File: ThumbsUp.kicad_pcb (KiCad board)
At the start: 2 copper layers, 215.3 x 230 mm, 51 parts, among them J1 52559-1233, J1L1 PJ-3200B, J1R1 PJ-3200B, J2 52559-1233, U1 ProMicro

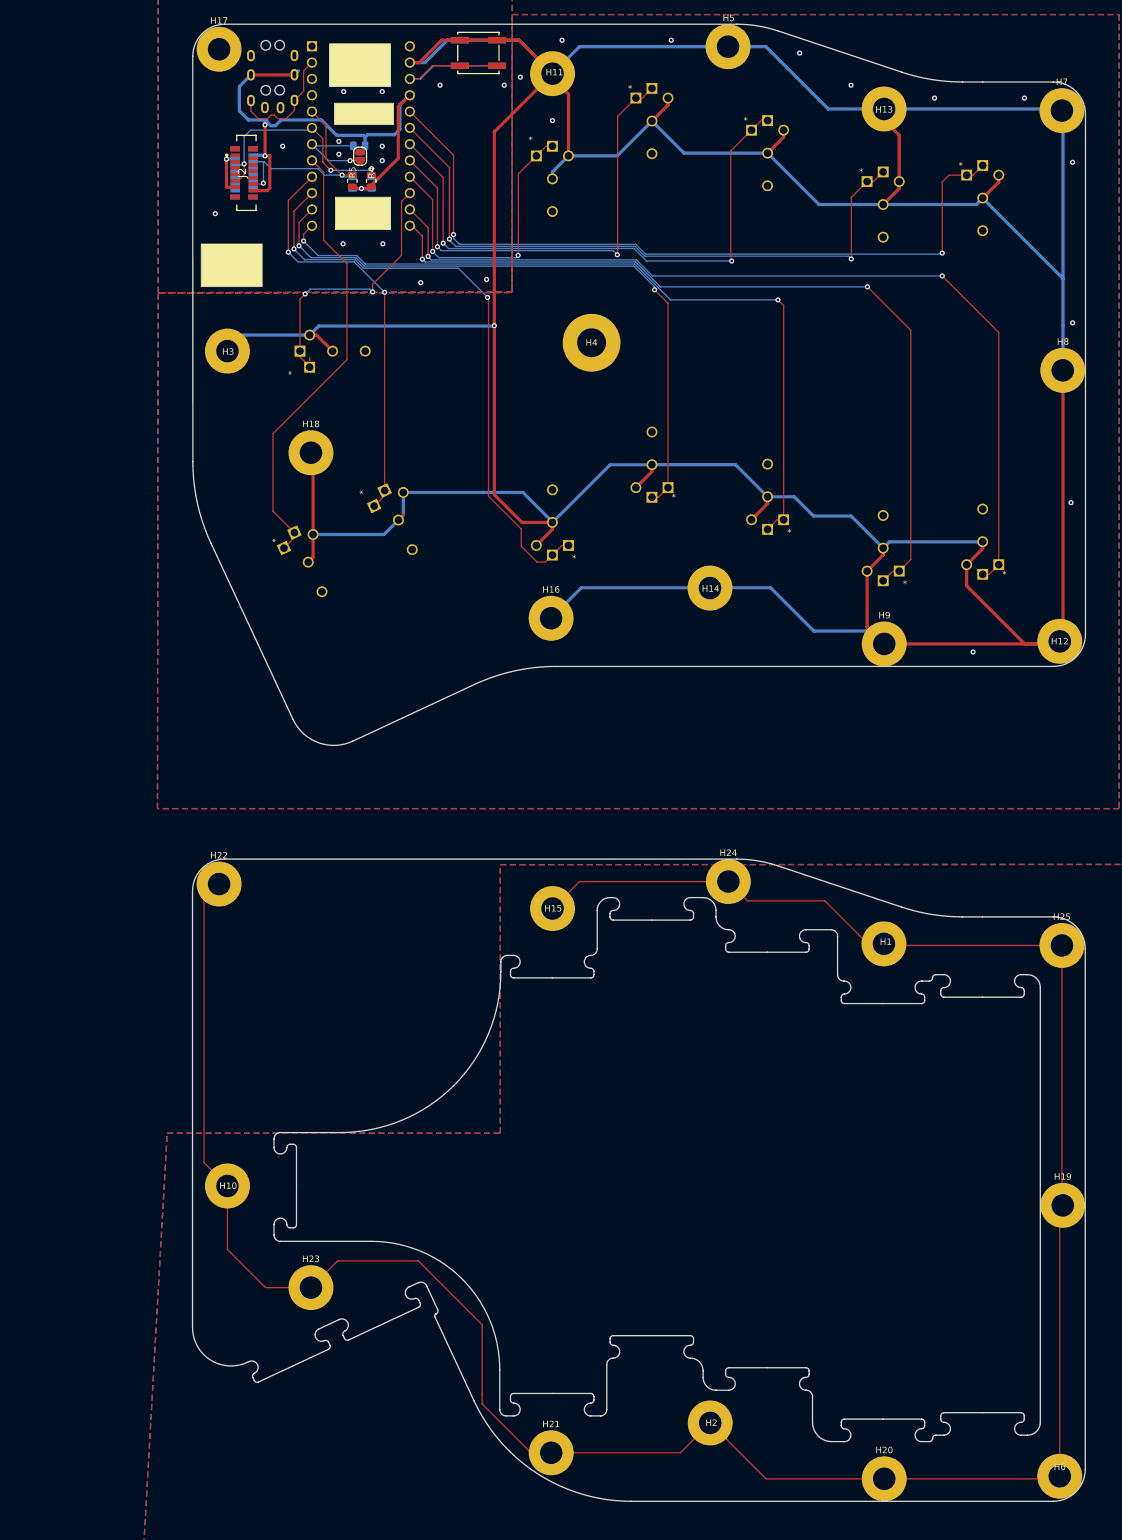
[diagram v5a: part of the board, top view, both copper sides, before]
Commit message: v12: Moving the thumb keys around.
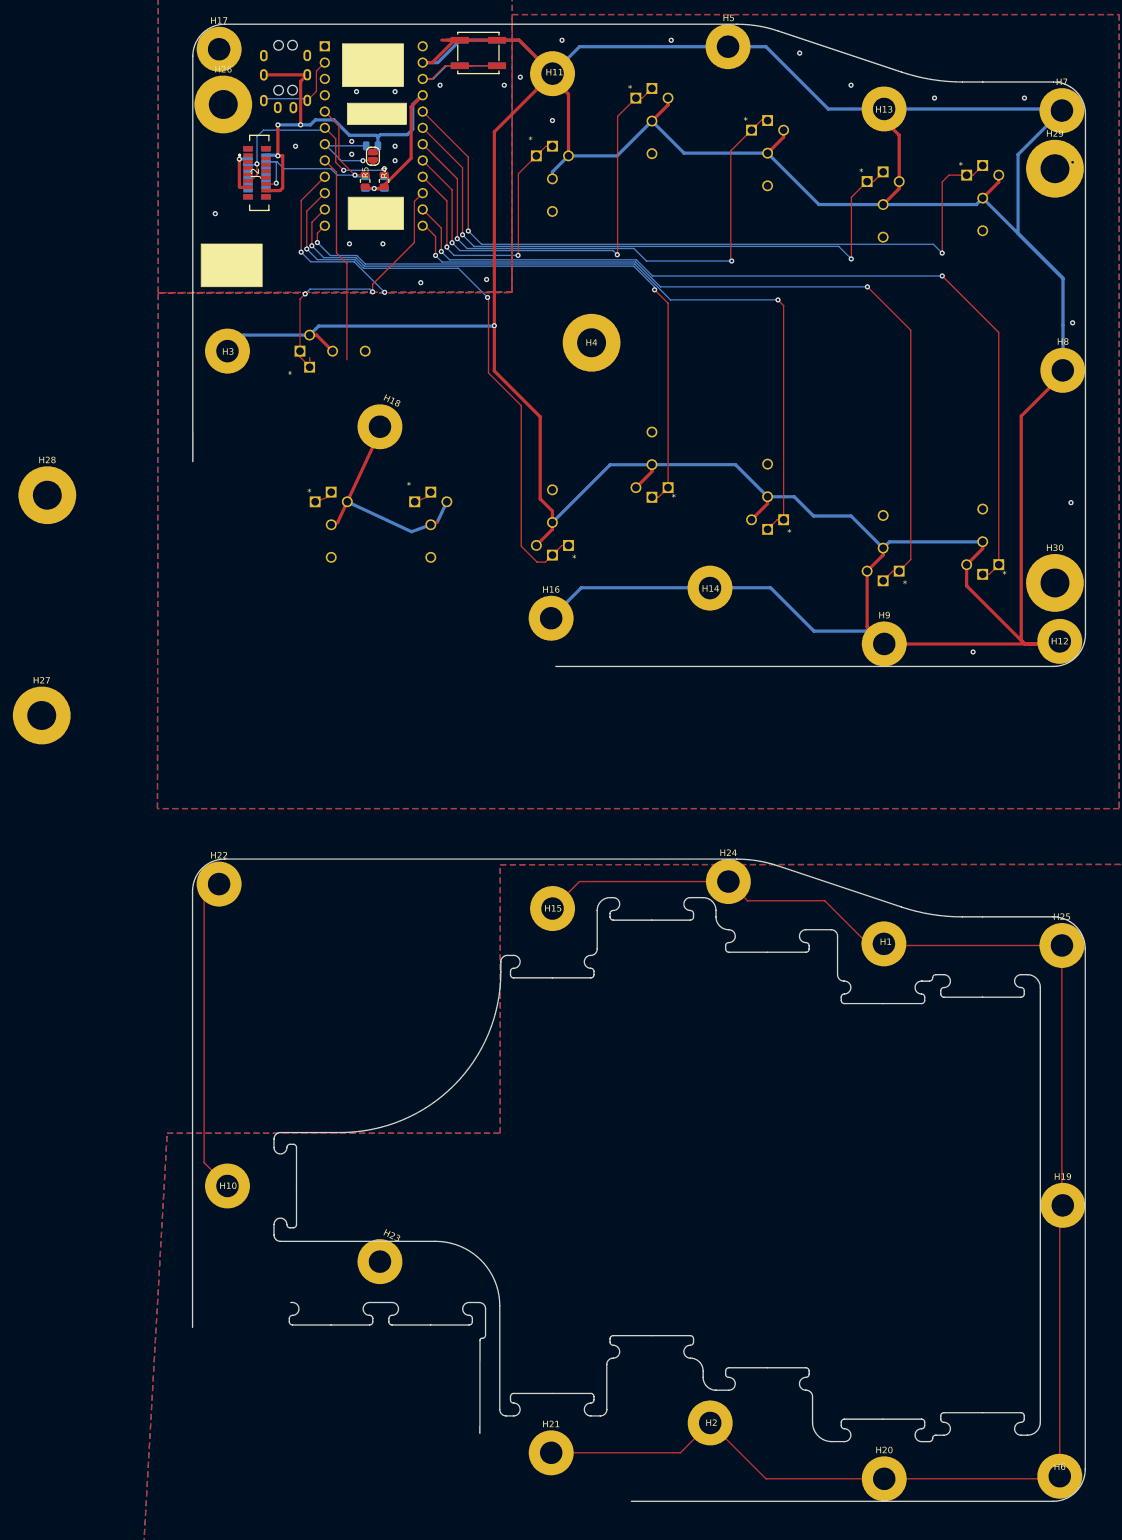
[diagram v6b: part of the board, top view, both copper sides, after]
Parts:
- added H26: MountingHole_Pad, MountingHole:MountingHole_4.5mm_Pad, F.Cu at (36.2, 38.0)
- added H27: MountingHole_Pad, MountingHole:MountingHole_4.5mm_Pad, F.Cu at (7.98, 133.1)
- added H28: MountingHole_Pad, MountingHole:MountingHole_4.5mm_Pad, F.Cu at (8.85, 98.8)
- added H29: MountingHole_Pad, MountingHole:MountingHole_4.5mm_Pad, F.Cu at (165.8, 48.0)
- added H30: MountingHole_Pad, MountingHole:MountingHole_4.5mm_Pad, F.Cu at (165.8, 112.5)
- moved H23 11.5 mm to (60.6, 218.2), turned to -25 degrees
- moved H18 11.5 mm to (60.6, 88.2), turned to -25 degrees
- moved MX30 8.52 mm to (53.1, 98.4), turned to 0 degrees
- moved MX26 7.19 mm to (68.6, 98.4), turned to 0 degrees
- moved J1 2.00 mm to (41.5, 48.6)
- moved J1L1 2.00 mm to (47.0, 27.2)
- moved J1R1 2.00 mm to (44.9, 27.2)
- moved J2 2.00 mm to (41.5, 48.6)
- moved JP1 2.00 mm to (59.6, 46.0)
- moved R1 2.00 mm to (58.4, 50.2)
- moved R17 2.00 mm to (59.4, 44.4)
- moved R2 2.00 mm to (61.3, 50.2)
- moved R4 2.00 mm to (61.3, 49.9)
- moved R5 2.00 mm to (58.3, 49.9)
- moved U1 2.00 mm to (59.7, 42.9)
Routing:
- net GNDA: track 389.6 -> 305.6 mm
- net SwE: track 69.4 -> 35.5 mm
- net SwU: track 64.8 -> 31.9 mm
- net GND: track 785.1 -> 765.4 mm
- net L-RING1: track 90.1 -> 84.9 mm, vias 3 -> 4
- net L-TIP: track 18.5 -> 14.0 mm
- net SwD: track 118.2 -> 115.2 mm
- net SwF: track 46.8 -> 43.9 mm
- net SwZ: track 141.8 -> 139.1 mm
- net SwL: track 88.6 -> 85.9 mm
- net SwP: track 72.5 -> 69.9 mm
- net SwT: track 100.0 -> 97.5 mm
- net SwS: track 128.2 -> 125.8 mm
- net SwG: track 118.3 -> 116.2 mm
- net SwR: track 93.2 -> 91.2 mm
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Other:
- outline, holes or cut-outs redrawn
- board text added: "u/ak66666 ThumbsUp! v.12 rev.5 June 2026"
- board text removed: "Raiser_Female"
- board text removed: "u/ak66666 ThumbsUp! v.12 rev.3 March 2026"

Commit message: v12: Added stand-offs instead of pin headers/sockets.
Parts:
- removed H29, H30: MountingHole_Pad, MountingHole:MountingHole_4.5mm_Pad
- added H31: MountingHole_Pad, MountingHole:MountingHole_3.5mm_Pad, F.Cu at (103.0, 26.4)
- added H32: MountingHole_Pad, MountingHole:MountingHole_3.5mm_Pad, F.Cu at (103.0, 108.2)
- added H33: MountingHole_Pad, MountingHole:MountingHole_3.5mm_Pad, F.Cu at (103.0, 156.4)
- added H34: MountingHole_Pad, MountingHole:MountingHole_3.5mm_Pad, F.Cu at (103.0, 238.2)
- moved H8 103.0 mm to (64.5, 88.9), turned to 15 degrees
- moved H19 102.9 mm to (64.5, 219.0), turned to 15 degrees
- moved H27 47.0 mm to (54.9, 130.6)
- moved H28 43.9 mm to (40.1, 68.0)
- moved H25 12.4 mm to (154.5, 169.4)
- moved H7 12.4 mm to (154.5, 39.5)
- moved H18 12.1 mm to (49.5, 93.0), turned to -10 degrees
- moved H23 12.1 mm to (49.6, 223.0), turned to -10 degrees
- moved H6 12.0 mm to (154.5, 251.2)
- moved H12 12.0 mm to (154.5, 121.2)
- moved H14 8.93 mm to (121.0, 113.2)
- moved H2 8.89 mm to (121.0, 243.1)
- moved H24 6.55 mm to (121.0, 161.4)
- moved H5 6.50 mm to (121.0, 31.4)
- moved H17 4.00 mm to (39.6, 29.4)
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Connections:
- H2 pad 1: GNDA -> GNDC
- H20 pad 1: GNDA -> GNDC
- H21 pad 1: GNDA -> GNDC
- H27 pad 1: GND-B -> GND
- H28 pad 1: GND-B -> GND
- H6 pad 1: GNDA -> GNDC
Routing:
- net GND: track 765.4 -> 599.5 mm
- net GNDA: track 305.6 -> 222.5 mm
- net GNDC: track 0.00 -> 79.2 mm
- net SwU: track 31.9 -> 64.1 mm
- net SwE: track 35.5 -> 61.1 mm
- net SwR: track 91.2 -> 85.8 mm
- net SwS: track 125.8 -> 121.0 mm
- net SwD: track 115.2 -> 110.8 mm
- net SwT: track 97.5 -> 93.8 mm
- net L-RING1: track 84.9 -> 88.5 mm, vias 4 -> 3
- net SwG: track 116.2 -> 113.2 mm
- net SwP: track 69.9 -> 66.9 mm
- net SwL: track 85.9 -> 82.9 mm
- net SwF: track 43.9 -> 40.9 mm
- net SwB: track 97.8 -> 94.8 mm
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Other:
- board size 215.3 x 230 mm -> 211.3 x 232.1 mm

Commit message: v12: Minor corrections.
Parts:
- removed H26, H28: MountingHole_Pad, MountingHole:MountingHole_4.5mm_Pad
- H27: footprint MountingHole:MountingHole_4.5mm_Pad -> MountingHole:MountingHole_3.5mm_Pad
- moved H27 1.22 mm to (54.3, 131.7)
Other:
- outline, holes or cut-outs redrawn
